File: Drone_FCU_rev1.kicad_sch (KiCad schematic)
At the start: 22 parts, among them J1 Conn_01x02_Pin, SW1 SW_Push, U1 STM32F722VETx, Y2 16MHz

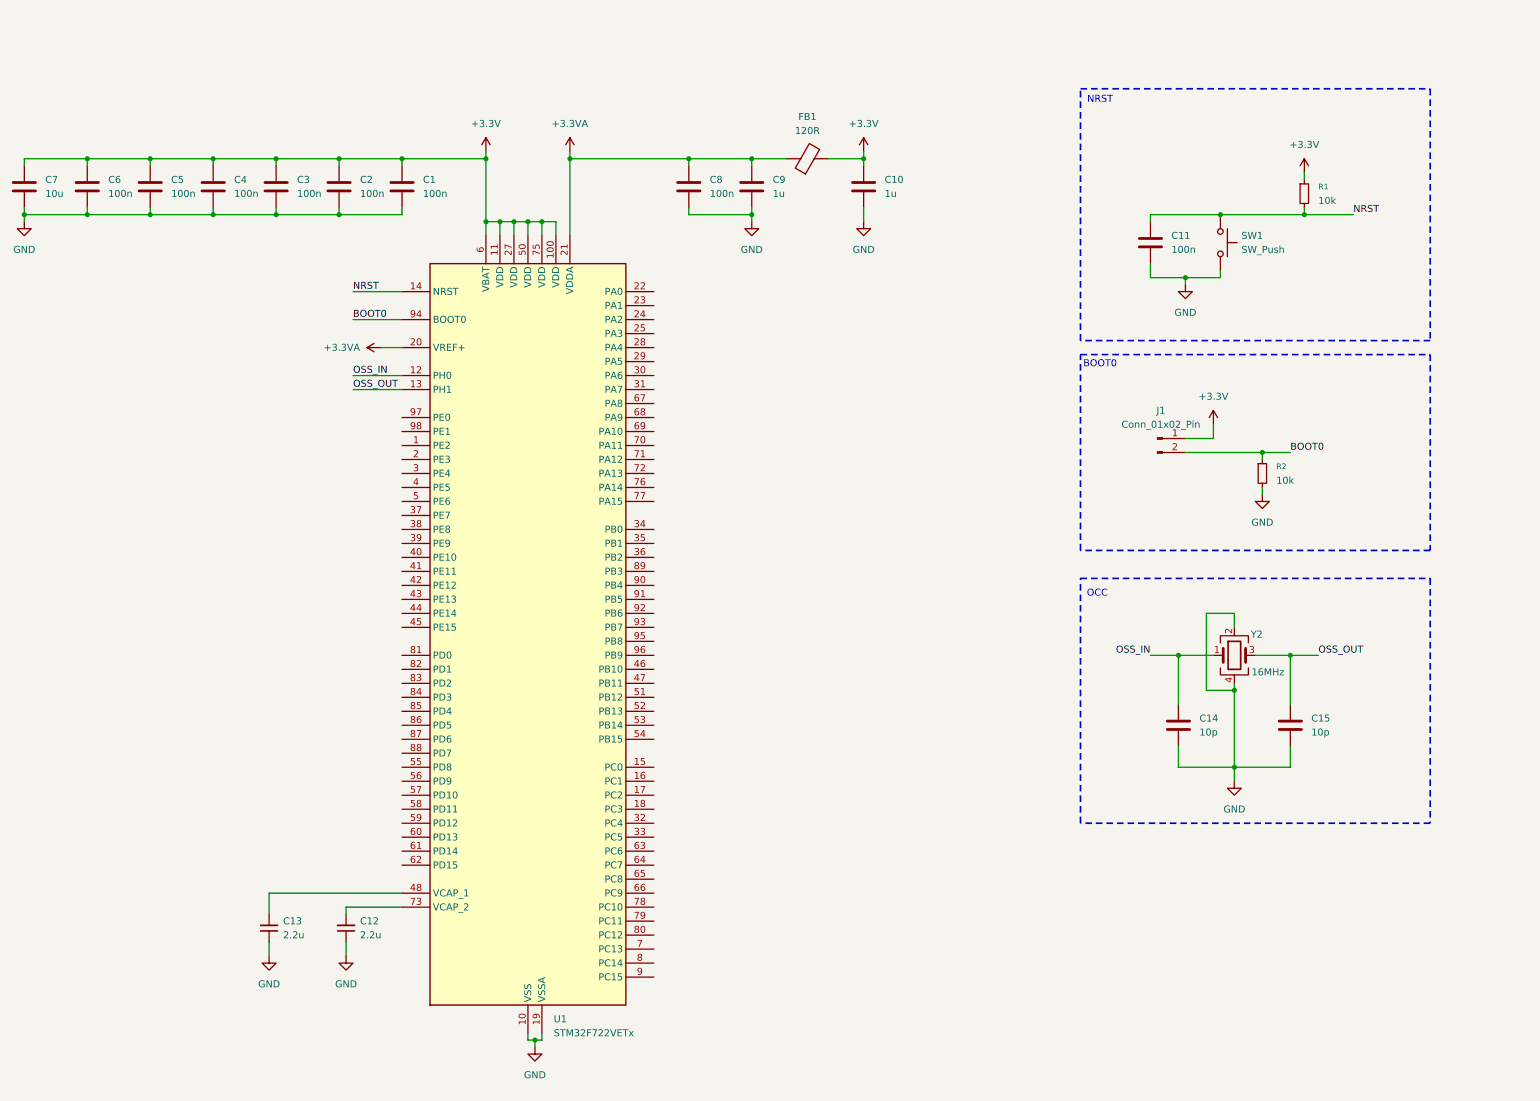
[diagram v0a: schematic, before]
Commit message: added usb otg and swd
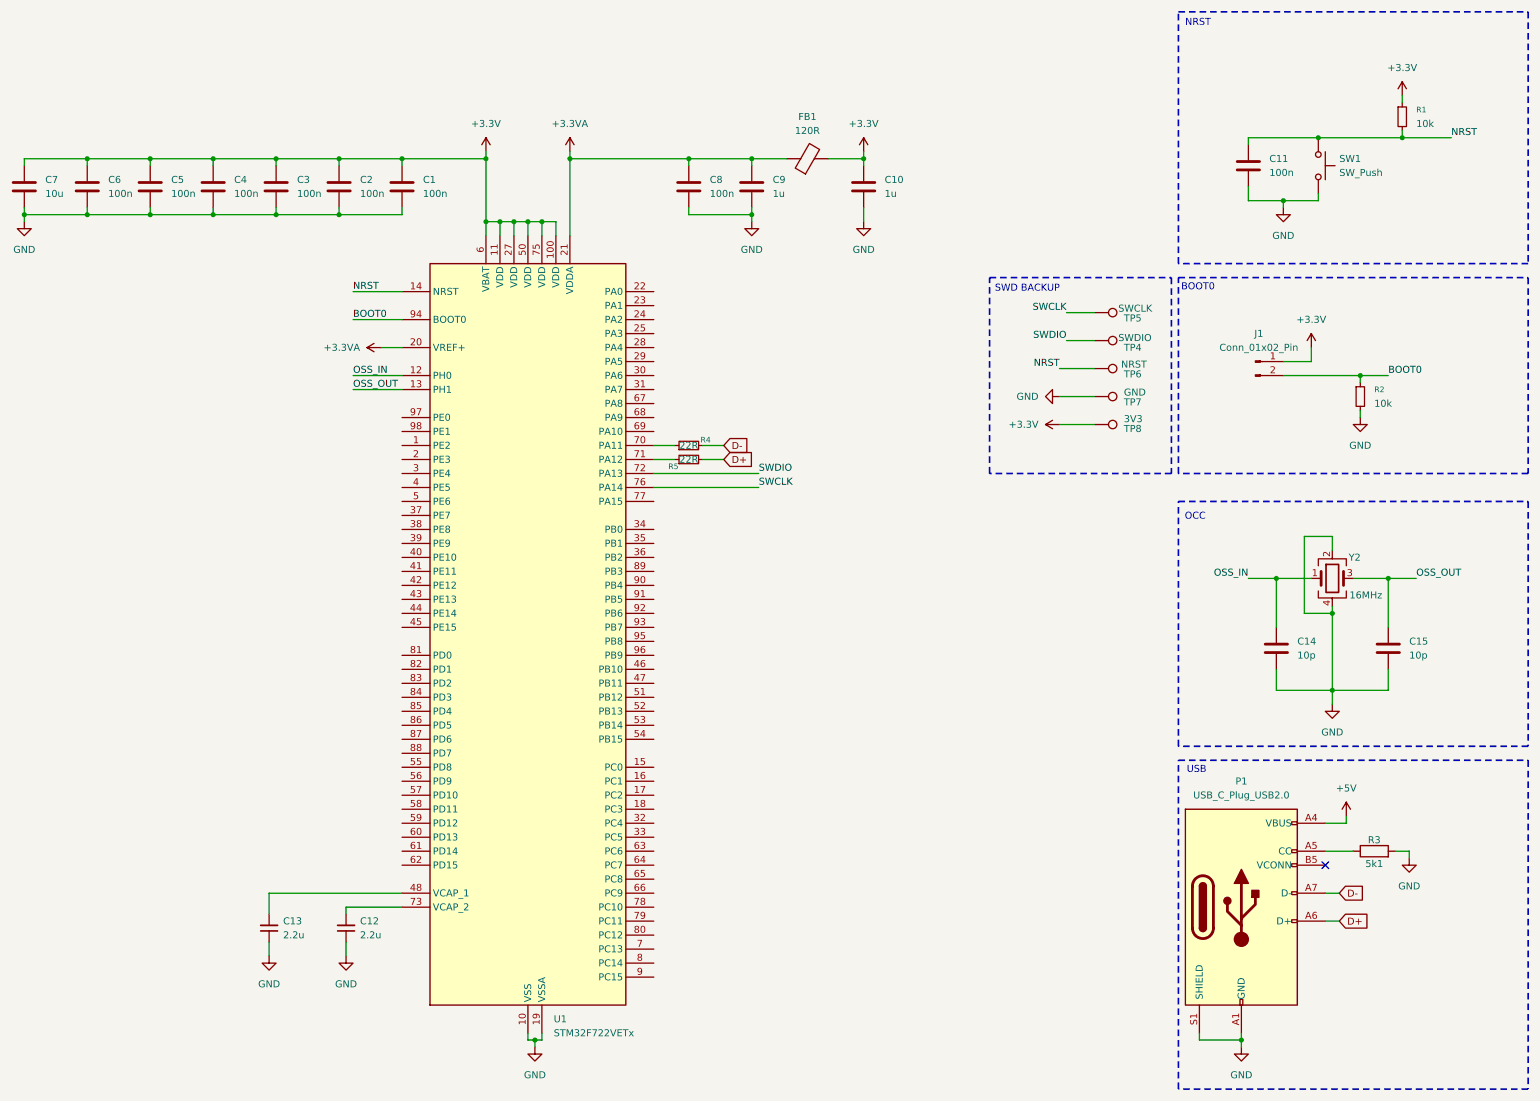
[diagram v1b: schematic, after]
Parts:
- added P1: USB_C_Plug_USB2.0, symbol Connector:USB_C_Plug_USB2.0
- added R3: 5k1, symbol Device:R
- added R4, R5: 22R, symbol Device:R_Small
- added TP4: SWDIO, symbol Connector:TestPoint
- added TP5: SWCLK, symbol Connector:TestPoint
- added TP6: NRST, symbol Connector:TestPoint
- added TP7: GND, symbol Connector:TestPoint
- added TP8: 3V3, symbol Connector:TestPoint
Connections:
- net +3.3V: now also TP8.1
- net GND: now also P1.A1 (GND), P1.A12 (GND), P1.B1 (GND), P1.B12 (GND), P1.S1 (SHIELD), R3.2, TP7.1
- net NRST: now also TP6.1
- net at U1.70 (PA11): now also R4.1
- net at U1.71 (PA12): now also R5.1
- net SWDIO: now reaches U1.72 (PA13)
- net SWDIO: now also TP4.1
- net SWCLK: now reaches U1.76 (PA14)
- net SWCLK: now also TP5.1
- new net: P1.A5 (CC), R3.1
- new net +5V: P1.A4 (VBUS), P1.A9 (VBUS), P1.B4 (VBUS), P1.B9 (VBUS)
- new net D+: P1.A6 (D+), R5.2
- new net D-: P1.A7 (D-), R4.2
- no-connect marks 0 -> 1
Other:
- note added: "SWD BACKUP"
- note added: "USB"
- moved on the sheet: C11, C14, C15, J1, R1, R2, SW1, Y2

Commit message: Updates
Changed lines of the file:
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@@
 	(wire
 		(pts
-			(xy 241.3 107.95) (xy 245.11 107.95)
-		)
-		(stroke
-			(width 0)
-			(type default)
-		)
-	)
-	(wire
-		(pts
 			(xy 232.41 113.03) (xy 251.46 113.03)
 		)
@@
 	(wire
 		(pts
-			(xy 241.3 105.41) (xy 245.11 105.41)
+			(xy 241.3 105.41) (xy 259.08 105.41)
 		)
 		(stroke
@@
 	(wire
 		(pts
+			(xy 261.62 105.41) (xy 261.62 107.95)
+		)
+		(stroke
+			(width 0)
+			(type default)
+		)
+	)
+	(wire
+		(pts
 			(xy 353.06 49.53) (xy 368.3 49.53)
 		)
@@
 	(wire
 		(pts
+			(xy 261.62 107.95) (xy 241.3 107.95)
+		)
+		(stroke
+			(width 0)
+			(type default)
+		)
+	)
+	(wire
+		(pts
 			(xy 209.55 212.09) (xy 209.55 213.36)
 		)
@@
 	(global_label "D+"
 		(shape input)
-		(at 245.11 107.95 0)
+		(at 261.62 105.41 90)
 		(fields_autoplaced yes)
 		(effects
@@
 		)
 		(property "Intersheetrefs" "${INTERSHEET_REFS}"
-			(at 250.9376 107.95 0)
+			(at 261.62 99.5824 90)
 			(effects
 				(font
@@
 	(global_label "D-"
 		(shape input)
-		(at 245.11 105.41 0)
+		(at 259.08 105.41 90)
 		(fields_autoplaced yes)
 		(effects
@@
 		)
 		(property "Intersheetrefs" "${INTERSHEET_REFS}"
-			(at 250.9376 105.41 0)
+			(at 259.08 99.5824 90)
 			(effects
 				(font
@@
 		)
 		(property "Value" "22R"
-			(at 238.76 107.95 90)
+			(at 238.76 109.728 90)
 			(effects
 				(font
@@
 		)
 		(property "Value" "22R"
-			(at 238.76 105.41 90)
+			(at 238.76 103.632 90)
 			(effects
 				(font
